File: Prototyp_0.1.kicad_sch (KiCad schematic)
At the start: 4 parts, among them U1 ESP32-S3-WROOM-1U

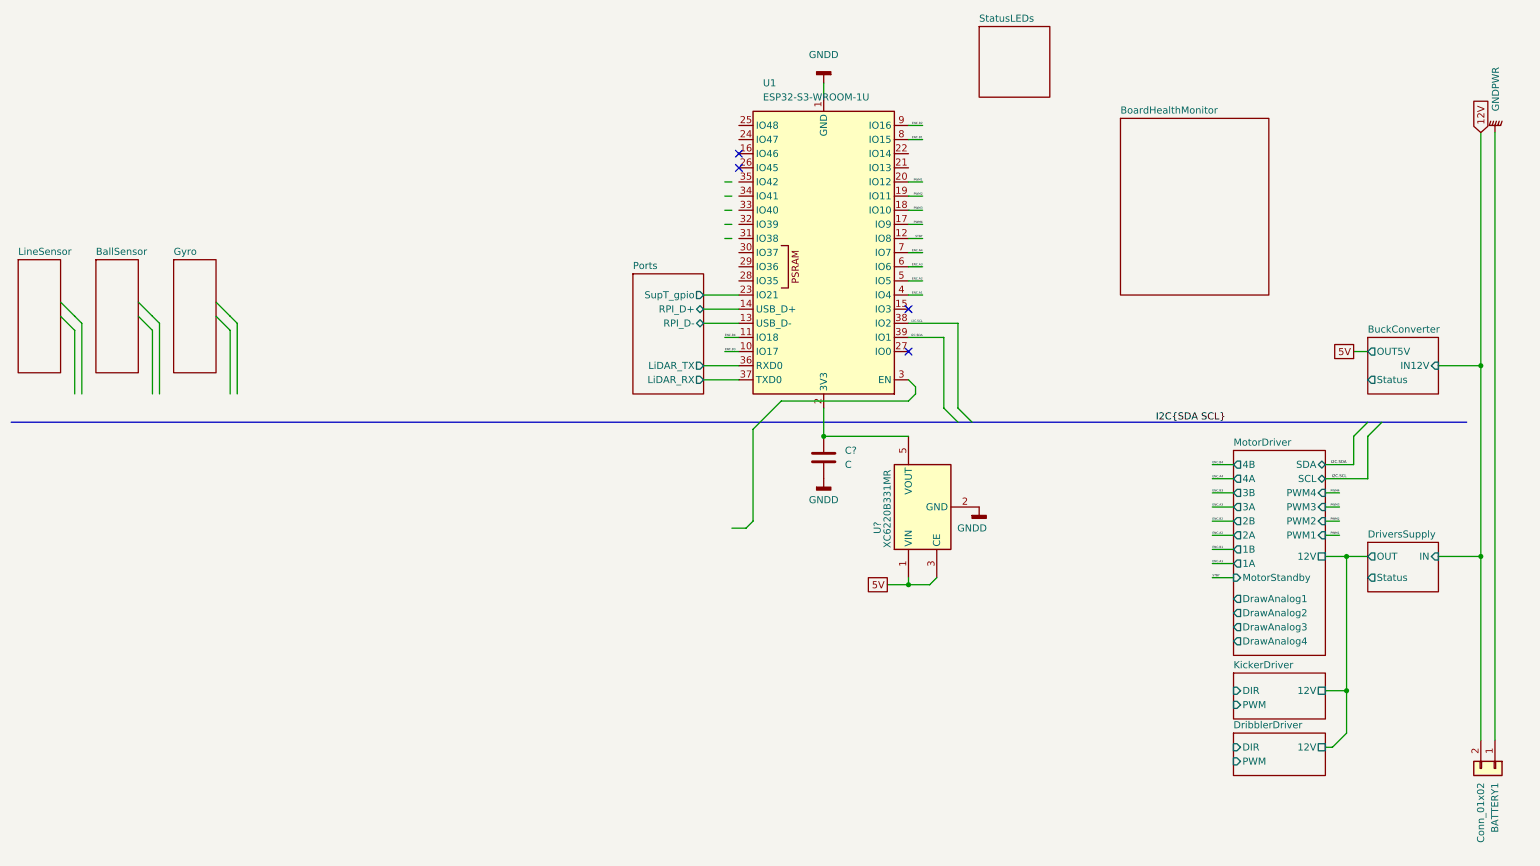
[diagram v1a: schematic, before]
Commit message: Added Libs folder and lib for eFuse
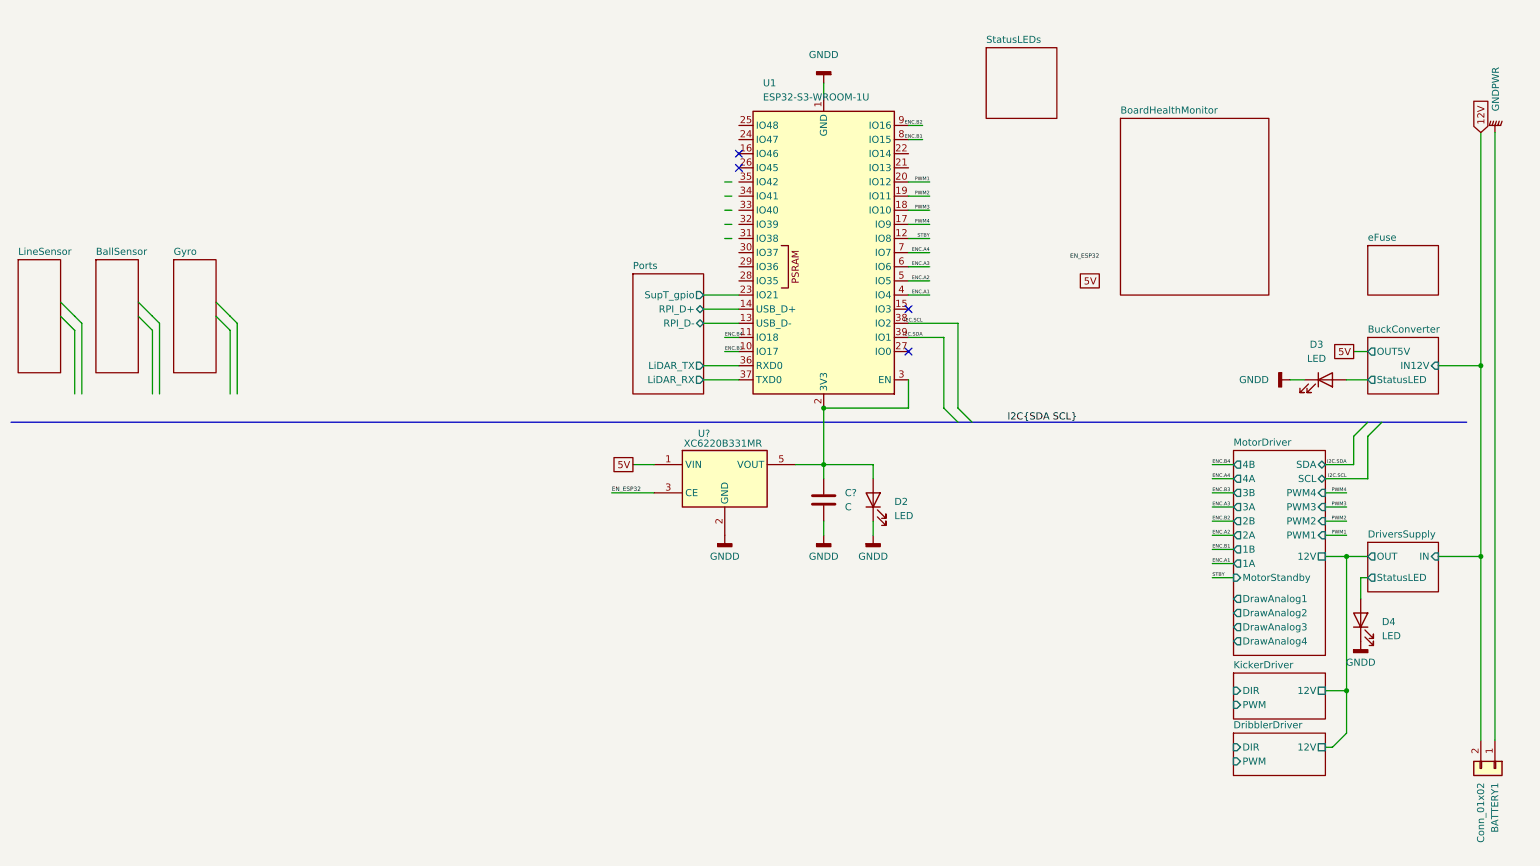
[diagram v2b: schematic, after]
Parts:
- added D2, D3, D4: LED, symbol Device:LED
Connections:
- net 5V: no longer U?.3 (CE)
- net GNDD: now also D2.1 (K), D3.1 (K), D4.1 (K)
- net at C?.1, U1.2 (3V3), U?.5 (VOUT): now also U1.3 (EN), D2.2 (A)
- new net BuckConverter/StatusLED: D3.2 (A)
- new net DriversSupply/StatusLED: D4.2 (A)
- new net EN_ESP32: U?.3 (CE)
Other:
- added sheet eFuse (./HierSheets/efuse.kicad_sch)
- sheet BuckConverter ports: added StatusLED; removed Status
- sheet DriversSupply ports: added StatusLED; removed Status
- moved on the sheet: C?, U?

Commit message: Efuse added, not set.
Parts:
- added D5: LED, symbol Device:LED
- added SW1: Killswitch, symbol Switch:SW_SPST
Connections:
- net 12V: no longer BATTERY1.2 (Pin_2)
- net GNDD: now also D5.1 (K)
- net GNDPWR: now also SW1.2 (B); no longer BATTERY1.1 (Pin_1)
- new net: BATTERY1.1 (Pin_1), SW1.1 (A)
- new net BuckConverter/12V: BATTERY1.2 (Pin_2)
- new net PowerGood: D5.2 (A)
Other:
- sheet BuckConverter ports: added 12V, 5V; removed IN12V, OUT5V
- sheet eFuse ports: added IN, OUT, Status; removed none

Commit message: Added kicker, interrupt, I2C pullups, buck converter, button
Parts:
- added R1, R2: 4.7kR, symbol Device:R
- added SW2: SW_Push, symbol Switch:SW_Push
- gave numbers to parts that had none: 2
- renumbered D2 to D1, D5 to D2, U1 to U2
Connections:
- net I2C.SDA is gone; now on net H_INTN: U2.39 (IO1)
- net 3V3: now reaches C1.1, D1.2 (A), U1.5 (VOUT), U2.2 (3V3), U2.3 (EN)
- net 3V3: now also R1.2, R2.2, SW2.1
- net KICKER: now reaches U2.21 (IO13)
- net H_INTN: now reaches U2.22 (IO14)
- net H_INTN: now also U2.38 (IO2), R1.1, R2.1
- net at U2.24 (IO47): now also SW2.2
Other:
- sheet BuckConverter ports: added 5_V_Raspberry; removed none
- sheet Gyro ports: added H_INTN, I2C.SCL, I2C.SDA; removed none
- sheet KickerDriver ports: added KICKER; removed DIR, PWM
- sheet LineSensor ports: added I2C.SCL, I2C.SDA; removed none
